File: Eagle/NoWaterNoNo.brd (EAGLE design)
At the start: 27 parts, among them U1 TINY85-20-DIP, U2 TINY85-20-DIP

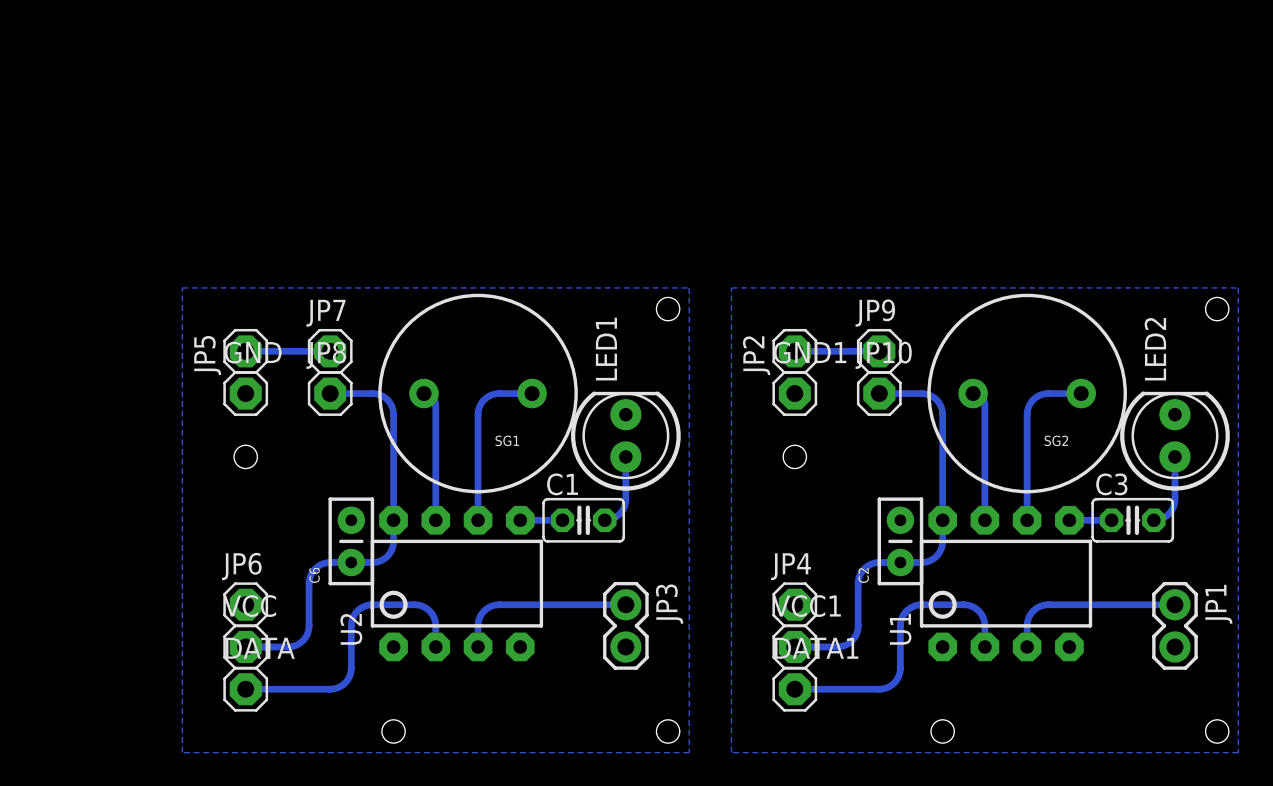
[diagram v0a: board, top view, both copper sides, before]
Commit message: Eagle: BRD and SCH files from test branch were more up to date than master.
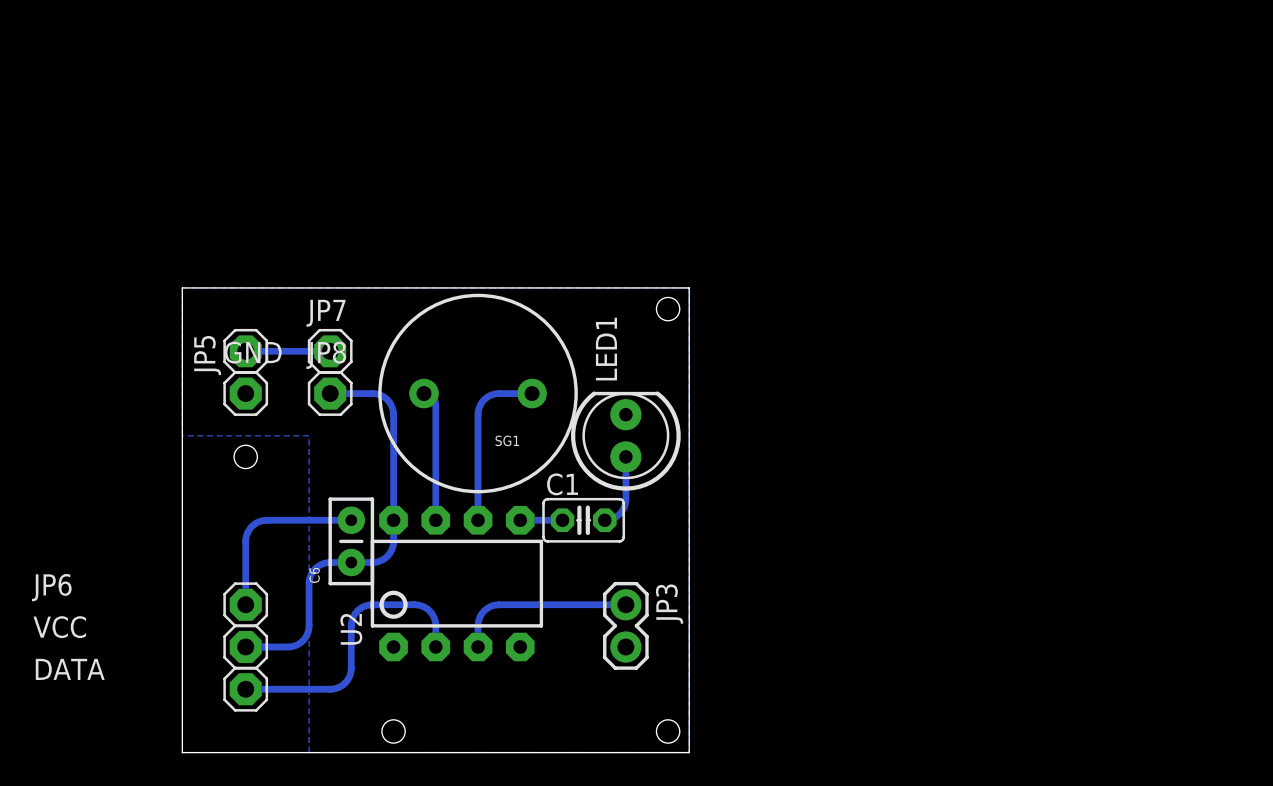
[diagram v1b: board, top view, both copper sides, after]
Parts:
- removed C2: 0.1uF, SparkFun:CAP-PTH-SMALL2
- removed C3: (no value), resistor:C025-025X050
- removed DATA1, GND1, JP10, JP2, JP4, JP9, VCC1: (no value), pinhead:1X01
- removed FRAME2: FRAME-LETTER, SparkFun-Aesthetics:CREATIVE_COMMONS
- removed JP1: Water Sensor, SparkFun-Connectors:1X02
- removed LED2: (no value), SparkFun-LED:LED5MM
- removed SG2: Buzzer, SparkFun-Electromechanical:BUZZER-12MM
- removed U1: TINY85-20-DIP, SparkFun-DigitalIC:DIP08
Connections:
- removed net D5: JP1.1, U1.3
- removed net D6: C3.1, U1.5
- removed net D7: SG2.-, U1.6
- removed net D8: SG2.+, U1.7
- removed net D9: DATA1.1, U1.2
- removed net GND1: C2.2, GND1.1, JP1.2, JP4.1, LED2.K, U1.4
- removed net N$2: C3.2, LED2.A
- removed net RESET1: U1.1
- removed net VCC1: C2.1, JP10.1, JP2.1, JP9.1, U1.8, VCC1.1
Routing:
- net VCC1: track 31.3 -> 0.00 mm
- net D9: track 16.8 -> 0.00 mm
- net GND: track 0.00 -> 10.7 mm
- net D5: track 10.7 -> 0.00 mm
- net D7: track 10.1 -> 0.00 mm
- net D8: track 7.91 -> 0.00 mm
- net N$2: track 4.34 -> 0.00 mm
- net D6: track 2.54 -> 0.00 mm
- removed copper zone on layer 16, net GND1
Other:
- board outline added: 30.5 x 27.9 mm

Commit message: Changed board layout. Buzzer, radio and sensor have changed pin assignments.
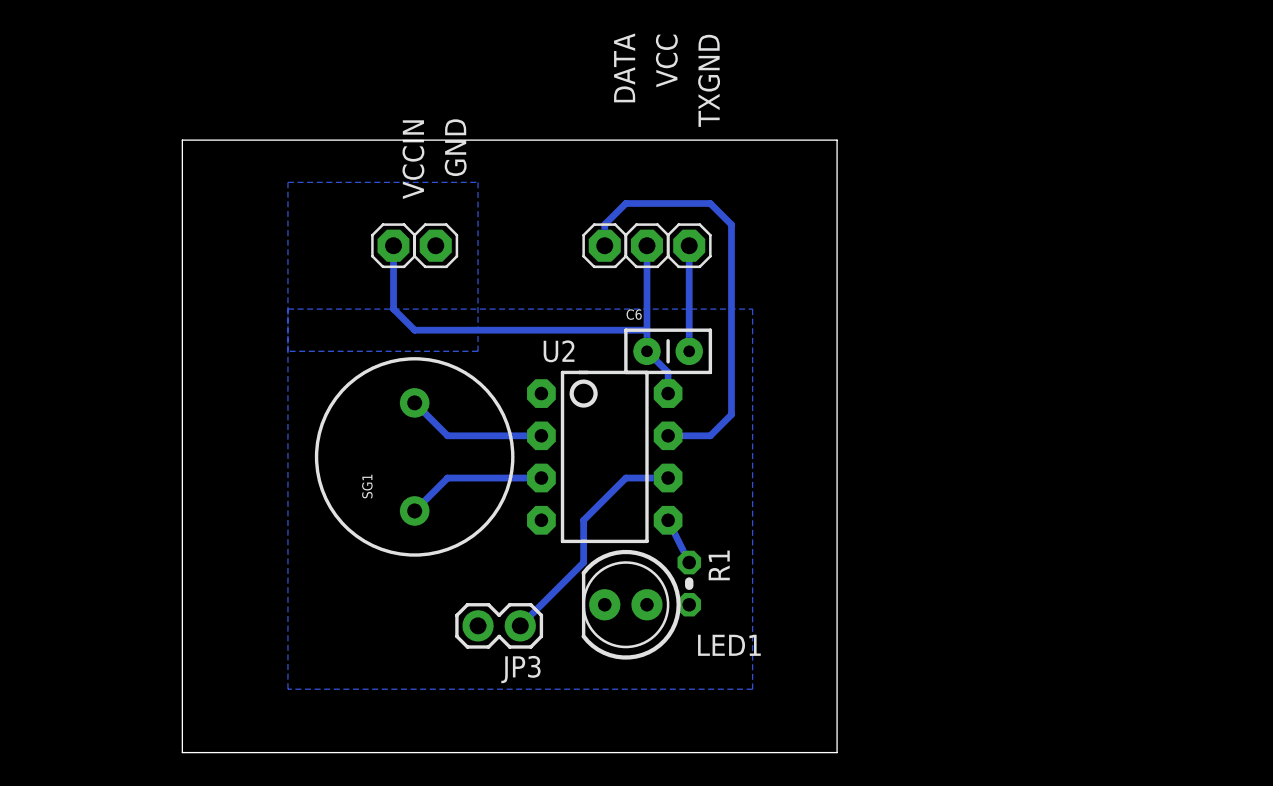
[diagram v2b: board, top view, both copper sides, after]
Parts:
- removed C1: (no value), resistor:C025-025X050
- removed JP5, JP6, JP7, JP8: (no value), pinhead:1X01
- added R1: (no value), rcl:0204V
- added TXGND, VCCIN: (no value), pinhead:1X01
- moved DATA 34.3 mm to (26.7, 31.8), turned to 270 degrees
- moved VCC 34.1 mm to (29.2, 31.8), turned to 270 degrees
- moved C6 21.8 mm to (29.2, 25.4), turned to 0 degrees
- moved GND 14.5 mm to (16.5, 31.8), turned to 270 degrees
- moved U2 11.7 mm to (26.7, 19.1), turned to 270 degrees
- moved LED1 10.2 mm to (27.9, 10.2), turned to 180 degrees
- moved JP3 6.48 mm to (21.6, 8.89), turned to 180 degrees
- moved SG1 5.39 mm to (15.2, 19.1), turned to 90 degrees
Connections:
- net D0: now also R1.1; no longer C1.1
- net D1: now also JP3.1; no longer SG1.-
- net D2: now also DATA.1; no longer SG1.+
- net D3: now also SG1.+; no longer DATA.1
- net D4: now also SG1.-; no longer JP3.1
- net GND: now also TXGND.1; no longer JP6.1
- net N$1: now also R1.2; no longer C1.2
- net VCC: now also VCCIN.1; no longer JP5.1, JP7.1, JP8.1
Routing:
- net D2: track 7.91 -> 25.7 mm
- net D3: track 16.8 -> 8.44 mm
- net N$1: track 4.34 -> 0.00 mm
- net GND: track 10.7 -> 6.35 mm
- net D1: track 10.1 -> 14.1 mm
- net VCC: track 31.3 -> 29.0 mm
- net D4: track 10.7 -> 8.44 mm
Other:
- board size 30.5 x 27.9 mm -> 39.4 x 36.8 mm

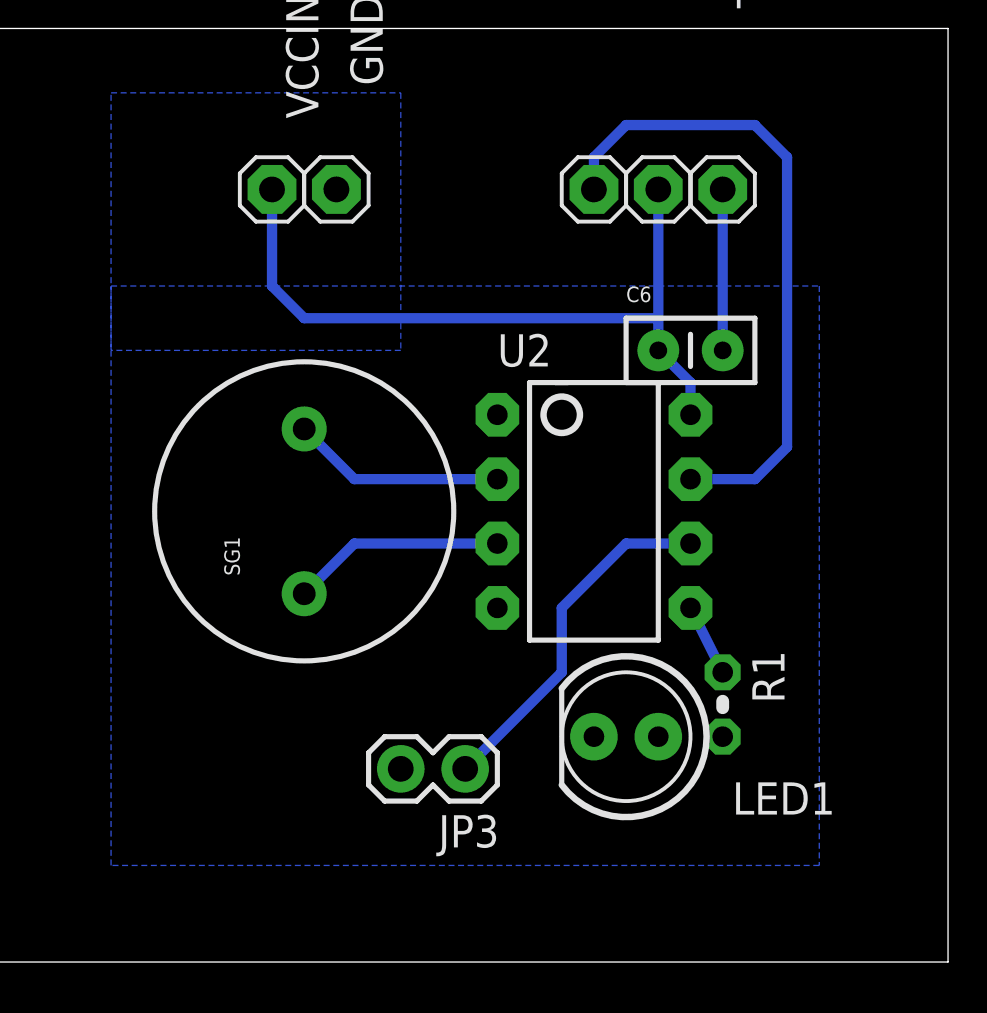
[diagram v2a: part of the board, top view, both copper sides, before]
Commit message: Changed board layouts once again. Changes made to Arduino code as well.
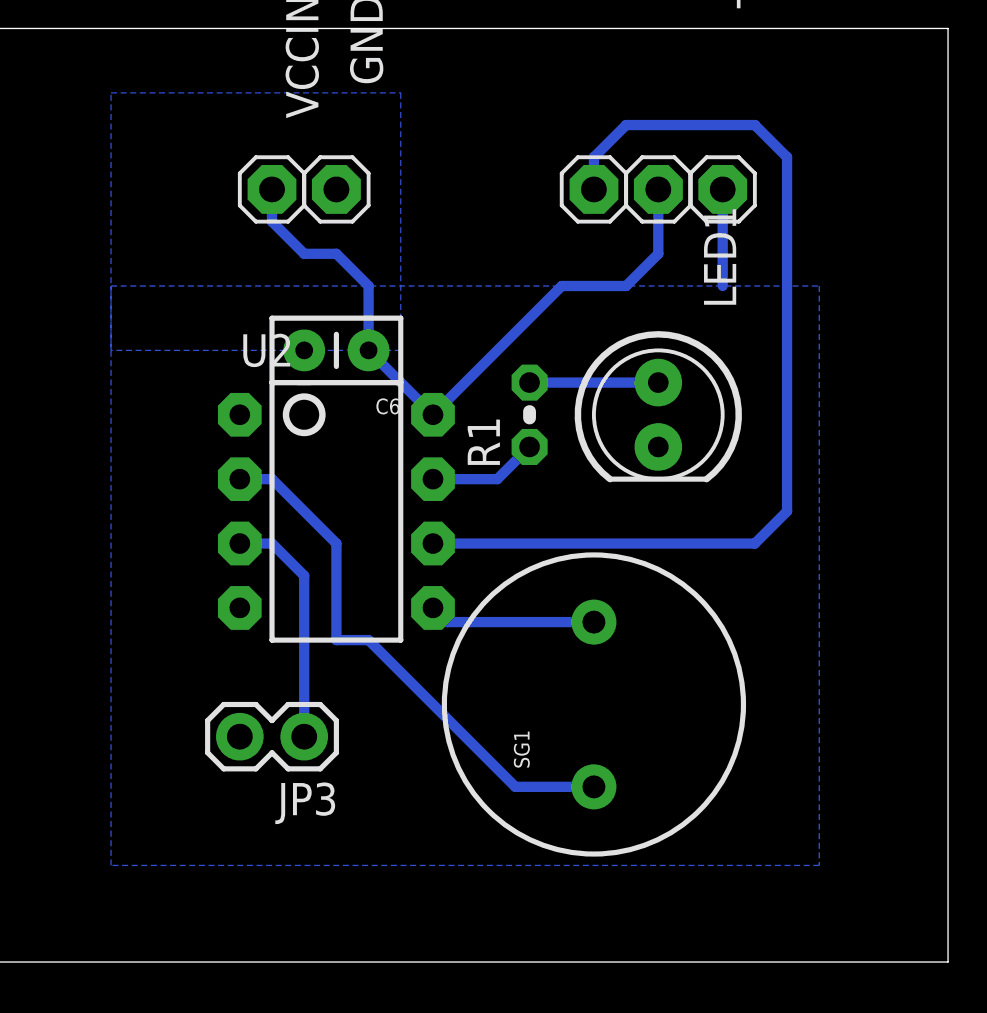
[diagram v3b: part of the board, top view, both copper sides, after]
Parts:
- moved SG1 13.7 mm to (26.7, 11.4)
- moved R1 13.7 mm to (24.1, 22.9), turned to 90 degrees
- moved LED1 12.8 mm to (29.2, 22.9), turned to 270 degrees
- moved C6 11.4 mm to (17.8, 25.4), turned to 180 degrees
- moved U2 10.2 mm to (16.5, 19.1)
- moved JP3 6.48 mm to (15.2, 10.2)
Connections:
- removed net D4: SG1.-, U2.3
- new net A2: JP3.1, U2.3
- net D0: now also SG1.+; no longer R1.1
- net D1: now also DATA.1; no longer JP3.1
- net D2: now also R1.1; no longer DATA.1
- net D3: now also SG1.-; no longer SG1.+
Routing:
- net D1: track 14.1 -> 38.4 mm
- net D2: track 25.7 -> 4.34 mm
- net D3: track 8.44 -> 21.2 mm
- net A2: track 0.00 -> 9.42 mm
- net D4: track 8.44 -> 0.00 mm
- net N$1: track 0.00 -> 5.08 mm
- net D0: track 2.84 -> 6.58 mm
- net VCC: track 29.0 -> 26.3 mm
- net GND: track 6.35 -> 3.81 mm
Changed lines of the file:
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@@
 </autorouter>
 <elements>
-<element name="C6" library="SparkFun" package="CAP-PTH-SMALL2" value="0.1uF" x="29.21" y="25.4" smashed="yes">
-<attribute name="NAME" x="27.94" y="27.305" size="0.6096" layer="25"/>
+<element name="C6" library="SparkFun" package="CAP-PTH-SMALL2" value="0.1uF" x="17.78" y="25.4" smashed="yes" rot="R180">
+<attribute name="NAME" x="19.05" y="23.495" size="0.6096" layer="25" rot="R180"/>
 </element>
-<element name="U2" library="SparkFun-DigitalIC" package="DIP08" value="TINY85-20-DIP" x="26.67" y="19.05" rot="R270">
-<attribute name="PROD_ID" value="IC-09445" x="26.67" y="19.05" size="1.778" layer="27" font="vector" ratio="15" rot="R270" display="off"/>
-<attribute name="VALUE" value="TINY85-20-DIP" x="26.67" y="19.05" size="1.778" layer="27" font="vector" ratio="15" rot="R270" display="off"/>
+<element name="U2" library="SparkFun-DigitalIC" package="DIP08" value="TINY85-20-DIP" x="16.51" y="19.05" rot="R270">
+<attribute name="PROD_ID" value="IC-09445" x="16.51" y="19.05" size="1.778" layer="27" font="vector" ratio="15" rot="R270" display="off"/>
+<attribute name="VALUE" value="TINY85-20-DIP" x="16.51" y="19.05" size="1.778" layer="27" font="vector" ratio="15" rot="R270" display="off"/>
 </element>
-<element name="JP3" library="SparkFun-Connectors" package="1X02" value="Water Sensor" x="21.59" y="8.89" rot="R180"/>
-<element name="LED1" library="SparkFun-LED" package="LED5MM" value="" x="27.94" y="10.16" smashed="yes" rot="R180">
-<attribute name="NAME" x="36.195" y="8.3566" size="1.27" layer="25" ratio="10" rot="R180"/>
-<attribute name="VALUE" x="24.7396" y="11.9634" size="1.27" layer="27" ratio="10" rot="R180"/>
+<element name="JP3" library="SparkFun-Connectors" package="1X02" value="Water Sensor" x="15.24" y="10.16" rot="R180"/>
+<element name="LED1" library="SparkFun-LED" package="LED5MM" value="" x="29.21" y="22.86" smashed="yes" rot="R270">
+<attribute name="NAME" x="31.0134" y="31.115" size="1.27" layer="25" ratio="10" rot="R270"/>
+<attribute name="VALUE" x="27.4066" y="19.6596" size="1.27" layer="27" ratio="10" rot="R270"/>
 </element>
-<element name="SG1" library="SparkFun-Electromechanical" package="BUZZER-12MM" value="Buzzer" x="15.24" y="19.05" rot="R90"/>
+<element name="SG1" library="SparkFun-Electromechanical" package="BUZZER-12MM" value="Buzzer" x="26.67" y="11.43" rot="R90"/>
 <element name="GND" library="pinhead" package="1X01" value="" x="16.51" y="31.75" smashed="yes" rot="R270">
 <attribute name="NAME" x="17.0688" y="39.4462" size="1.27" layer="25" ratio="10" rot="R270"/>
@@
 <attribute name="VALUE" x="28.575" y="33.02" size="1.27" layer="27" rot="R270"/>
 </element>
-<element name="R1" library="rcl" package="0204V" value="" x="31.75" y="11.43" rot="R270"/>
+<element name="R1" library="rcl" package="0204V" value="" x="24.13" y="22.86" rot="R90"/>
 </elements>
 <signals>
@@
 <vertex x="19.05" y="25.4"/>
 </polygon>
-<wire x1="31.75" y1="31.75" x2="31.75" y2="25.4" width="0.4064" layer="16"/>
+<wire x1="31.75" y1="31.75" x2="31.75" y2="27.94" width="0.4064" layer="16"/>
 </signal>
 <signal name="VCC">
@@
 <contactref element="VCC" pad="1"/>
 <contactref element="VCCIN" pad="1"/>
-<wire x1="13.97" y1="31.75" x2="13.97" y2="27.94" width="0.4064" layer="16"/>
-<wire x1="13.97" y1="27.94" x2="15.24" y2="26.67" width="0.4064" layer="16"/>
-<wire x1="30.48" y1="22.86" x2="30.48" y2="24.13" width="0.4064" layer="16"/>
-<wire x1="30.48" y1="24.13" x2="29.21" y2="25.4" width="0.4064" layer="16"/>
-<wire x1="29.21" y1="31.75" x2="29.21" y2="26.67" width="0.4064" layer="16"/>
-<wire x1="29.21" y1="26.67" x2="29.21" y2="25.4" width="0.4064" layer="16"/>
-<wire x1="15.24" y1="26.67" x2="29.21" y2="26.67" width="0.4064" layer="16"/>
+<wire x1="13.97" y1="31.75" x2="13.97" y2="30.48" width="0.4064" layer="16"/>
+<wire x1="13.97" y1="30.48" x2="15.24" y2="29.21" width="0.4064" layer="16"/>
+<wire x1="15.24" y1="29.21" x2="16.51" y2="29.21" width="0.4064" layer="16"/>
+<wire x1="16.51" y1="29.21" x2="17.78" y2="27.94" width="0.4064" layer="16"/>
+<wire x1="17.78" y1="27.94" x2="17.78" y2="25.4" width="0.4064" layer="16"/>
+<wire x1="17.78" y1="25.4" x2="20.32" y2="22.86" width="0.4064" layer="16"/>
+<wire x1="29.21" y1="31.75" x2="29.21" y2="29.21" width="0.4064" layer="16"/>
+<wire x1="29.21" y1="29.21" x2="27.94" y2="27.94" width="0.4064" layer="16"/>
+<wire x1="27.94" y1="27.94" x2="25.4" y2="27.94" width="0.4064" layer="16"/>
+<wire x1="25.4" y1="27.94" x2="20.32" y2="22.86" width="0.4064" layer="16"/>
 </signal>
 <signal name="RESET">
 <contactref element="U2" pad="1"/>
 </signal>
-<signal name="D4">
-<contactref element="U2" pad="3"/>
-<contactref element="SG1" pad="-"/>
-<wire x1="22.86" y1="17.78" x2="17.22" y2="17.78" width="0.4064" layer="16"/>
-<wire x1="17.22" y1="17.78" x2="15.24" y2="15.8" width="0.4064" layer="16"/>
-</signal>
 <signal name="D0">
 <contactref element="U2" pad="5"/>
-<contactref element="R1" pad="1"/>
-<wire x1="30.48" y1="15.24" x2="31.75" y2="12.7" width="0.4064" layer="16"/>
+<contactref element="SG1" pad="+"/>
+<wire x1="20.32" y1="15.24" x2="20.88" y2="14.68" width="0.4064" layer="16"/>
+<wire x1="20.88" y1="14.68" x2="26.67" y2="14.68" width="0.4064" layer="16"/>
 </signal>
 <signal name="D3">
 <contactref element="U2" pad="2"/>
-<contactref element="SG1" pad="+"/>
-<wire x1="22.86" y1="20.32" x2="17.22" y2="20.32" width="0.4064" layer="16"/>
-<wire x1="17.22" y1="20.32" x2="15.24" y2="22.3" width="0.4064" layer="16"/>
+<contactref element="SG1" pad="-"/>
+<wire x1="12.7" y1="20.32" x2="13.97" y2="20.32" width="0.4064" layer="16"/>
+<wire x1="13.97" y1="20.32" x2="16.51" y2="17.78" width="0.4064" layer="16"/>
+<wire x1="16.51" y1="17.78" x2="16.51" y2="13.97" width="0.4064" layer="16"/>
+<wire x1="16.51" y1="13.97" x2="17.78" y2="13.97" width="0.4064" layer="16"/>
+<wire x1="17.78" y1="13.97" x2="23.57" y2="8.18" width="0.4064" layer="16"/>
+<wire x1="23.57" y1="8.18" x2="26.67" y2="8.18" width="0.4064" layer="16"/>
 </signal>
 <signal name="N$1">
 <contactref element="R1" pad="2"/>
 <contactref element="LED1" pad="A"/>
-<wire x1="29.21" y1="10.16" x2="31.75" y2="10.16" width="0" layer="19" extent="1-1"/>
+<wire x1="24.13" y1="24.13" x2="29.21" y2="24.13" width="0.4064" layer="16"/>
 </signal>
 <signal name="D1">
 <contactref element="U2" pad="6"/>
-<contactref element="JP3" pad="1"/>
-<wire x1="21.59" y1="8.89" x2="25.4" y2="12.7" width="0.4064" layer="16"/>
-<wire x1="25.4" y1="12.7" x2="25.4" y2="15.24" width="0.4064" layer="16"/>
-<wire x1="25.4" y1="15.24" x2="27.94" y2="17.78" width="0.4064" layer="16"/>
-<wire x1="27.94" y1="17.78" x2="30.48" y2="17.78" width="0.4064" layer="16"/>
-</signal>
-<signal name="D2">
-<contactref element="U2" pad="7"/>
 <contactref element="DATA" pad="1"/>
-<wire x1="30.48" y1="20.32" x2="33.02" y2="20.32" width="0.4064" layer="16"/>
-<wire x1="33.02" y1="20.32" x2="34.29" y2="21.59" width="0.4064" layer="16"/>
-<wire x1="34.29" y1="21.59" x2="34.29" y2="33.02" width="0.4064" layer="16"/>
+<wire x1="20.32" y1="17.78" x2="33.02" y2="17.78" width="0.4064" layer="16"/>
+<wire x1="33.02" y1="17.78" x2="34.29" y2="19.05" width="0.4064" layer="16"/>
+<wire x1="34.29" y1="19.05" x2="34.29" y2="33.02" width="0.4064" layer="16"/>
 <wire x1="34.29" y1="33.02" x2="33.02" y2="34.29" width="0.4064" layer="16"/>
 <wire x1="33.02" y1="34.29" x2="27.94" y2="34.29" width="0.4064" layer="16"/>
@@
 <wire x1="26.67" y1="33.02" x2="26.67" y2="31.75" width="0.4064" layer="16"/>
 </signal>
+<signal name="D2">
+<contactref element="U2" pad="7"/>
+<contactref element="R1" pad="1"/>
+<wire x1="20.32" y1="20.32" x2="22.86" y2="20.32" width="0.4064" layer="16"/>
+<wire x1="22.86" y1="20.32" x2="24.13" y2="21.59" width="0.4064" layer="16"/>
+</signal>
+<signal name="A2">
+<contactref element="JP3" pad="1"/>
+<contactref element="U2" pad="3"/>
+<wire x1="12.7" y1="17.78" x2="13.97" y2="17.78" width="0.4064" layer="16"/>
+<wire x1="13.97" y1="17.78" x2="15.24" y2="16.51" width="0.4064" layer="16"/>
+<wire x1="15.24" y1="16.51" x2="15.24" y2="10.16" width="0.4064" layer="16"/>
+</signal>
 </signals>
